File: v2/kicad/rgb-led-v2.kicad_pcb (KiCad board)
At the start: 2 copper layers, 90 x 50 mm, 11 parts

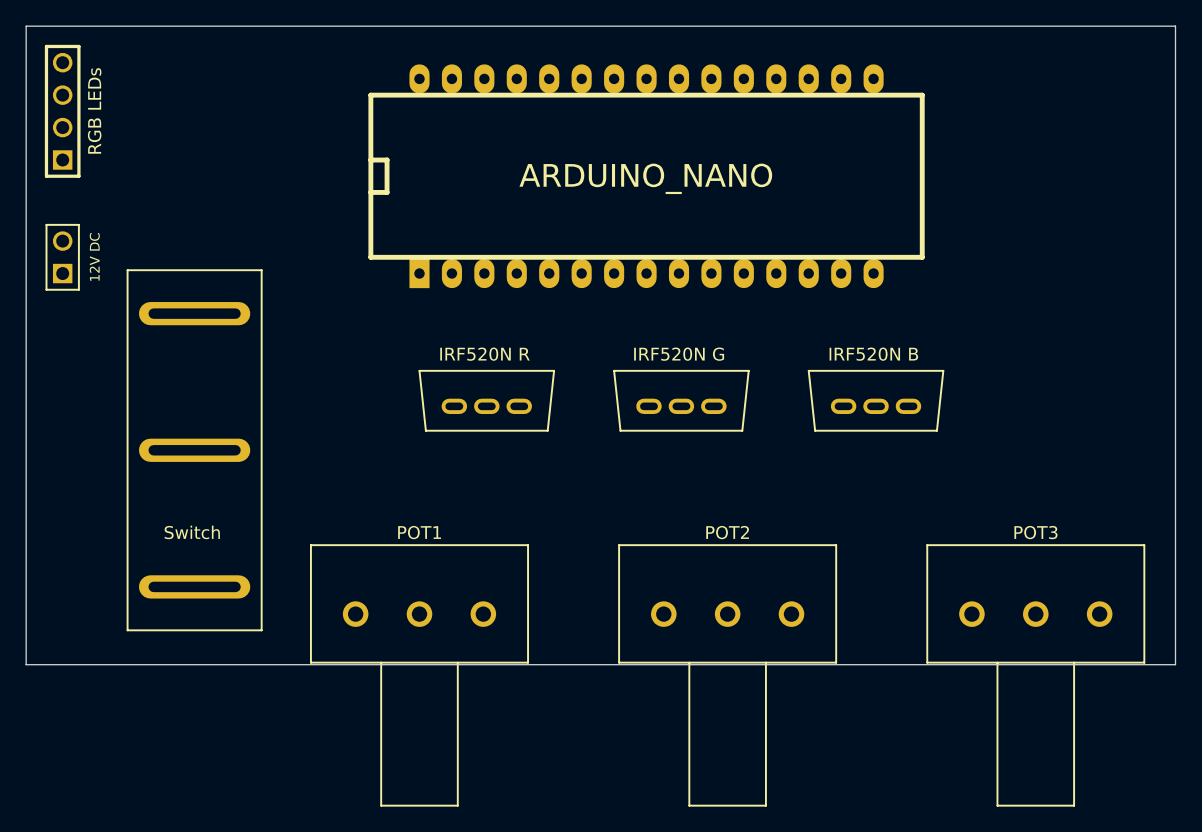
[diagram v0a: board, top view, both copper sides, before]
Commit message: [v2] Fixed references in PCB layout
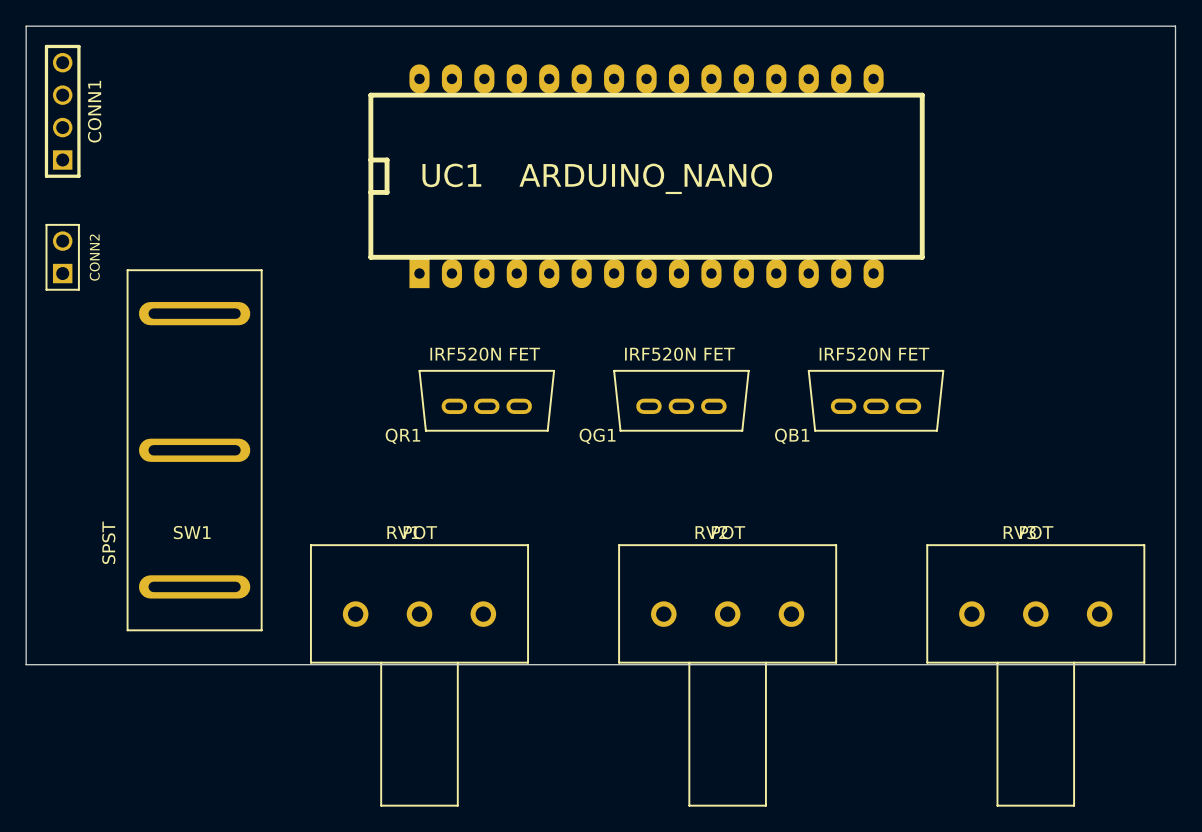
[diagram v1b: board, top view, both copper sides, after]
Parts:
- CONN1: renamed from RGB LEDs
- CONN2: renamed from 12V DC
- QB1: renamed from ?; value IRF520N B -> IRF520N FET
- QG1: renamed from ?; value IRF520N G -> IRF520N FET
- QR1: renamed from ?; value IRF520N R -> IRF520N FET
- RV1: renamed from ?; value POT1 -> POT
- RV2: renamed from ?; value POT2 -> POT
- RV3: renamed from ?; value POT3 -> POT
- SW1: renamed from Switch; value (none) -> SPST
- gave numbers to parts that had none: 1
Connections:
- QB1 pad D: (no net) -> N-0000016
- QB1 pad G: (no net) -> N-000004
- QB1 pad S: (no net) -> GND
- QG1 pad D: (no net) -> N-000005
- QG1 pad G: (no net) -> N-000001
- QG1 pad S: (no net) -> GND
- QR1 pad D: (no net) -> N-0000011
- QR1 pad G: (no net) -> N-000003
- QR1 pad S: (no net) -> GND
- SW1 pad 1: (no net) -> N-0000019
- SW1 pad 2: (no net) -> N-0000017
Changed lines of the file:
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@@
 (kicad_pcb (version 3) (host pcbnew "(2013-may-18)-stable")
   (general
-    (links 11)
-    (no_connects 11)
+    (links 22)
+    (no_connects 22)
     (area 18.679999 19.949999 115.369049 81.130001)
     (thickness 1.6)
@@
   (module POT_3 (layer F.Cu)
     (at 49.53 66.04)
-    (fp_text reference "" (at -1.27 -6.35) (layer F.SilkS)
-      (effects (font (size 1 1) (thickness 0.15)))
-    )
-    (fp_text value POT1 (at 0 -6.35) (layer F.SilkS)
+    (fp_text reference RV1 (at -1.27 -6.35) (layer F.SilkS)
+      (effects (font (size 1 1) (thickness 0.15)))
+    )
+    (fp_text value POT (at 0 -6.35) (layer F.SilkS)
       (effects (font (size 1 1) (thickness 0.15)))
     )
@@
   (module POT_3 (layer F.Cu)
     (at 73.66 66.04)
-    (fp_text reference "" (at -1.27 -6.35) (layer F.SilkS)
-      (effects (font (size 1 1) (thickness 0.15)))
-    )
-    (fp_text value POT2 (at 0 -6.35) (layer F.SilkS)
+    (fp_text reference RV2 (at -1.27 -6.35) (layer F.SilkS)
+      (effects (font (size 1 1) (thickness 0.15)))
+    )
+    (fp_text value POT (at 0 -6.35) (layer F.SilkS)
       (effects (font (size 1 1) (thickness 0.15)))
     )
@@
   (module POT_3 (layer F.Cu)
     (at 97.79 66.04)
-    (fp_text reference "" (at -1.27 -6.35) (layer F.SilkS)
-      (effects (font (size 1 1) (thickness 0.15)))
-    )
-    (fp_text value POT3 (at 0 -6.35) (layer F.SilkS)
+    (fp_text reference RV3 (at -1.27 -6.35) (layer F.SilkS)
+      (effects (font (size 1 1) (thickness 0.15)))
+    )
+    (fp_text value POT (at 0 -6.35) (layer F.SilkS)
       (effects (font (size 1 1) (thickness 0.15)))
     )
@@
     (descr "Double rangee de contacts 2 x 5 pins")
     (tags CONN)
-    (fp_text reference "RGB LEDs" (at 0 2.54 90) (layer F.SilkS)
+    (fp_text reference CONN1 (at 0 2.54 90) (layer F.SilkS)
       (effects (font (size 1.016 1.016) (thickness 0.2032)))
     )
@@
     (descr "Connecteurs 2 pins")
     (tags "CONN DEV")
-    (fp_text reference "12V DC" (at 0 2.54 90) (layer F.SilkS)
+    (fp_text reference CONN2 (at 0 2.54 90) (layer F.SilkS)
       (effects (font (size 0.762 0.762) (thickness 0.1524)))
     )
@@
   (module KCD3 (layer F.Cu)
     (at 26.67 67.31 90)
-    (fp_text reference Switch (at 7.62 5.08 180) (layer F.SilkS)
-      (effects (font (size 1 1) (thickness 0.15)))
-    )
-    (fp_text value "" (at 6.8072 -1.4351 90) (layer F.SilkS)
+    (fp_text reference SW1 (at 7.62 5.08 180) (layer F.SilkS)
+      (effects (font (size 1 1) (thickness 0.15)))
+    )
+    (fp_text value SPST (at 6.8072 -1.4351 90) (layer F.SilkS)
       (effects (font (size 1 1) (thickness 0.15)))
     )
@@
     (pad 1 thru_hole oval (at 3.4 5.25 90) (size 1.82 8.72) (drill oval 0.82 7.22)
       (layers *.Cu *.Mask F.SilkS)
+      (net 9 N-0000019)
     )
     (pad 2 thru_hole oval (at 14.1 5.25 90) (size 1.82 8.72) (drill oval 0.82 7.22)
       (layers *.Cu *.Mask F.SilkS)
+      (net 8 N-0000017)
     )
     (pad 3 thru_hole oval (at 24.8 5.25 90) (size 1.82 8.72) (drill oval 0.82 7.22)
@@
     (descr "30 pins DIL package, elliptical pads, width 600mil (arduino nano)")
     (tags "DIL arduino nano")
-    (fp_text reference "" (at -16.51 0) (layer F.SilkS)
+    (fp_text reference UC1 (at -16.51 0) (layer F.SilkS)
       (effects (font (size 1.778 1.778) (thickness 0.3048)))
     )
@@
   (module IRF520N (layer F.Cu)
     (at 49.53 46.99)
-    (fp_text reference "" (at -1.27 5.08) (layer F.SilkS)
-      (effects (font (size 1 1) (thickness 0.15)))
-    )
-    (fp_text value "IRF520N R" (at 5.08 -1.27) (layer F.SilkS)
+    (fp_text reference QR1 (at -1.27 5.08) (layer F.SilkS)
+      (effects (font (size 1 1) (thickness 0.15)))
+    )
+    (fp_text value "IRF520N FET" (at 5.08 -1.27) (layer F.SilkS)
       (effects (font (size 1 1) (thickness 0.15)))
     )
@@
     (pad G thru_hole oval (at 2.73 2.78) (size 2 1.2) (drill oval 1.4 0.6)
       (layers *.Cu *.Mask F.SilkS)
+      (net 11 N-000003)
     )
     (pad D thru_hole oval (at 5.27 2.78) (size 2 1.2) (drill oval 1.4 0.6)
       (layers *.Cu *.Mask F.SilkS)
+      (net 4 N-0000011)
     )
     (pad S thru_hole oval (at 7.81 2.78) (size 2 1.2) (drill oval 1.4 0.6)
       (layers *.Cu *.Mask F.SilkS)
+      (net 1 GND)
     )
   )
   (module IRF520N (layer F.Cu)
     (at 64.77 46.99)
-    (fp_text reference "" (at -1.27 5.08) (layer F.SilkS)
-      (effects (font (size 1 1) (thickness 0.15)))
-    )
-    (fp_text value "IRF520N G" (at 5.08 -1.27) (layer F.SilkS)
+    (fp_text reference QG1 (at -1.27 5.08) (layer F.SilkS)
+      (effects (font (size 1 1) (thickness 0.15)))
+    )
+    (fp_text value "IRF520N FET" (at 5.08 -1.27) (layer F.SilkS)
       (effects (font (size 1 1) (thickness 0.15)))
     )
@@
     (pad G thru_hole oval (at 2.73 2.78) (size 2 1.2) (drill oval 1.4 0.6)
       (layers *.Cu *.Mask F.SilkS)
+      (net 2 N-000001)
     )
     (pad D thru_hole oval (at 5.27 2.78) (size 2 1.2) (drill oval 1.4 0.6)
       (layers *.Cu *.Mask F.SilkS)
+      (net 13 N-000005)
     )
     (pad S thru_hole oval (at 7.81 2.78) (size 2 1.2) (drill oval 1.4 0.6)
       (layers *.Cu *.Mask F.SilkS)
+      (net 1 GND)
     )
   )
   (module IRF520N (layer F.Cu)
     (at 80.01 46.99)
-    (fp_text reference "" (at -1.27 5.08) (layer F.SilkS)
-      (effects (font (size 1 1) (thickness 0.15)))
-    )
-    (fp_text value "IRF520N B" (at 5.08 -1.27) (layer F.SilkS)
+    (fp_text reference QB1 (at -1.27 5.08) (layer F.SilkS)
+      (effects (font (size 1 1) (thickness 0.15)))
+    )
+    (fp_text value "IRF520N FET" (at 5.08 -1.27) (layer F.SilkS)
       (effects (font (size 1 1) (thickness 0.15)))
     )
@@
     (pad G thru_hole oval (at 2.73 2.78) (size 2 1.2) (drill oval 1.4 0.6)
       (layers *.Cu *.Mask F.SilkS)
+      (net 12 N-000004)
     )
     (pad D thru_hole oval (at 5.27 2.78) (size 2 1.2) (drill oval 1.4 0.6)
       (layers *.Cu *.Mask F.SilkS)
+      (net 7 N-0000016)
     )
     (pad S thru_hole oval (at 7.81 2.78) (size 2 1.2) (drill oval 1.4 0.6)
       (layers *.Cu *.Mask F.SilkS)
-    )
-  )
+      (net 1 GND)
+    )
+  )

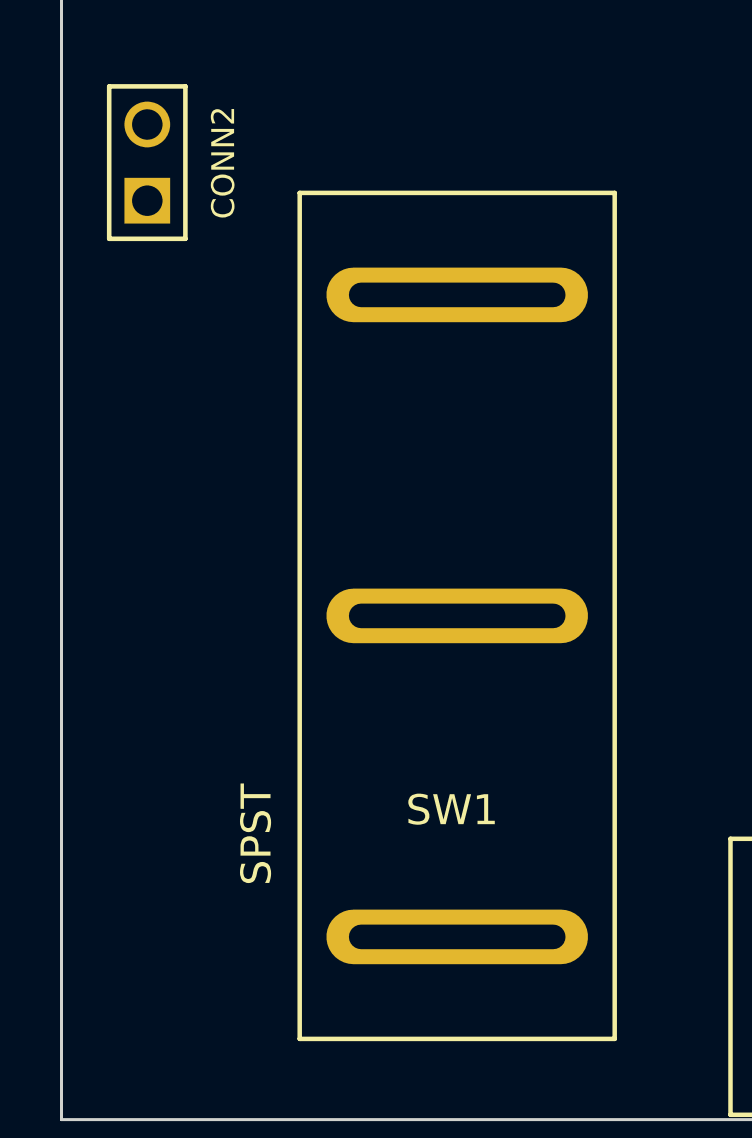
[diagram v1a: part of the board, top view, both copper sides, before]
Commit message: [v2] Configured track widths
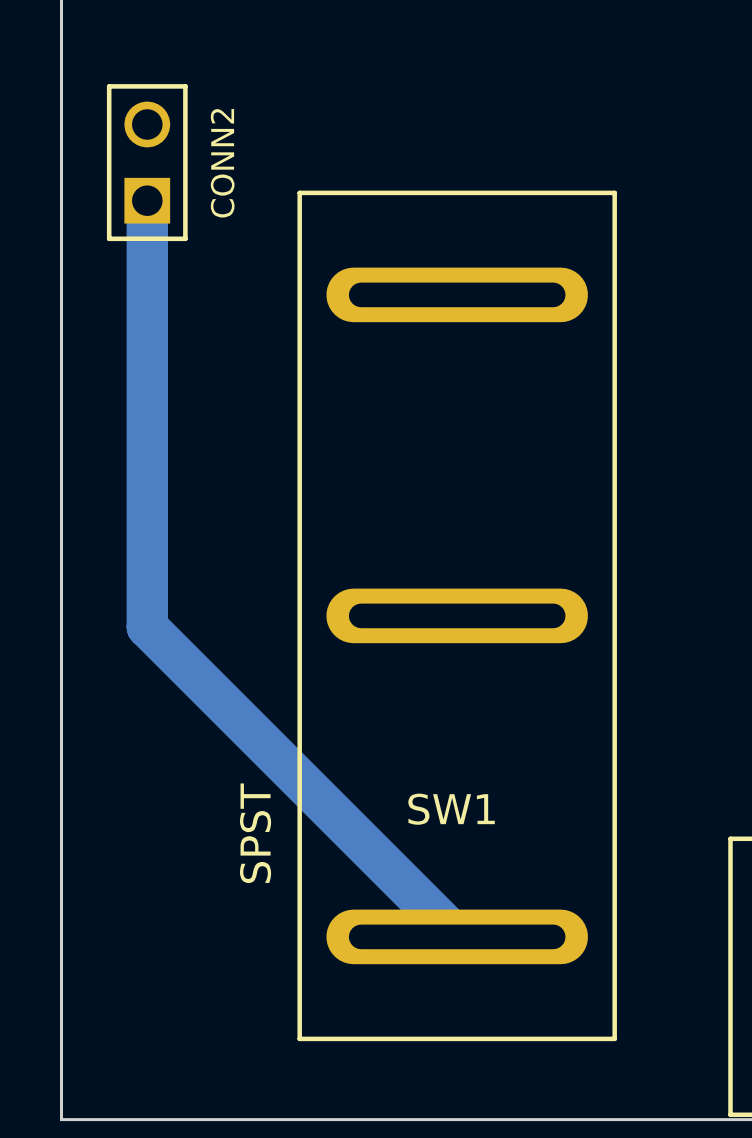
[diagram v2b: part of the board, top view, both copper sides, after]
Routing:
- net N-0000019: track 0.00 -> 28.8 mm
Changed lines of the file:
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@@
   (general
     (links 22)
-    (no_connects 22)
+    (no_connects 21)
     (area 18.679999 19.949999 115.369049 81.130001)
     (thickness 1.6)
     (drawings 6)
-    (tracks 0)
+    (tracks 2)
     (zones 0)
     (modules 11)
@@
   )
   (setup
-    (last_trace_width 0.01)
+    (last_trace_width 1.38)
+    (user_trace_width 0.035)
+    (user_trace_width 0.35)
+    (user_trace_width 1.38)
     (trace_clearance 0.015)
     (zone_clearance 0.508)
@@
   (gr_line (start 108.73 20) (end 108.73 70) (angle 90) (layer Edge.Cuts) (width 0.1))
   (gr_line (start 18.73 70) (end 108.73 70) (angle 90) (layer Edge.Cuts) (width 0.1))
+  (segment (start 21.59 39.37) (end 21.59 53.58) (width 1.38) (layer B.Cu) (net 9) (status 400000))
+  (segment (start 21.59 53.58) (end 31.92 63.91) (width 1.38) (layer B.Cu) (net 9) (status 800000))
 )

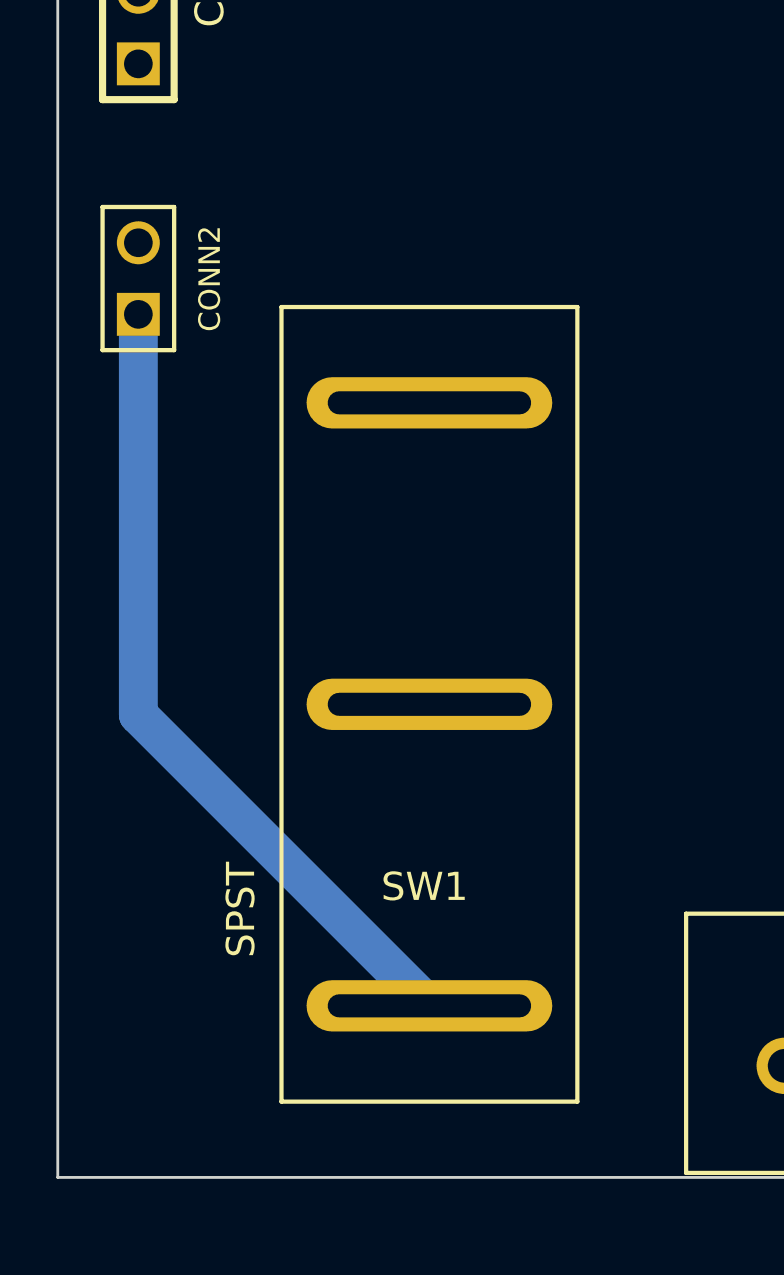
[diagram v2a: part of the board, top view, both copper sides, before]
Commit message: [v2] Added fuse
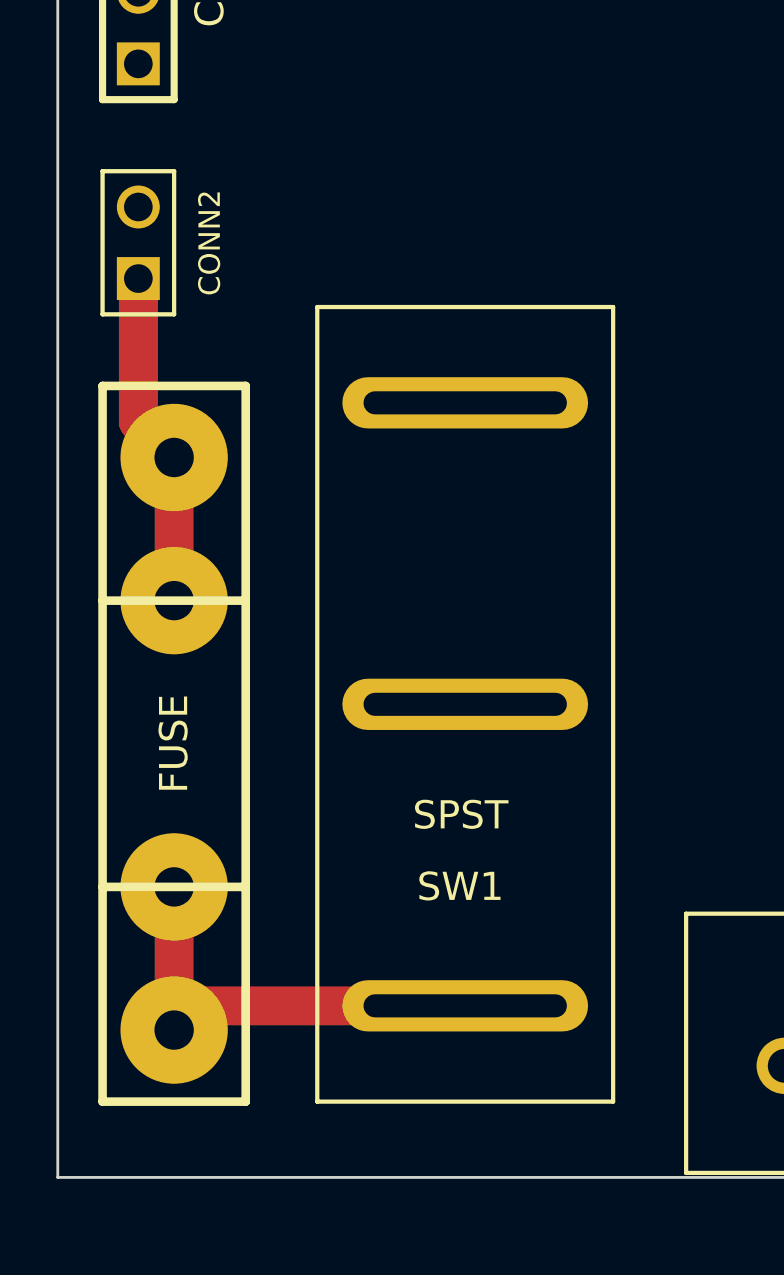
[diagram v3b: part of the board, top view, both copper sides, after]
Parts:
- added F1: FUSE, FUSE5-20, F.Cu at (22.9, 54.6)
- moved CONN2 1.27 mm to (21.6, 36.8)
- moved SW1 1.27 mm to (27.9, 67.3)
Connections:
- CONN2 pad 1: N-0000019 -> N-000009
- SW1 pad 1: N-0000019 -> N-000002
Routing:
- net N-0000019: track 28.8 -> 0.00 mm
- net N-000002: track 0.00 -> 15.8 mm
- net N-000009: track 0.00 -> 12.0 mm

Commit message: [v2] PCB Routing
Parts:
- moved QB1 15.2 mm to (64.8, 47.0)
- moved QG1 15.2 mm to (80.0, 47.0)
- moved G*** 3.17 mm to (36.8, 28.6)
- turned UC1 to 180 degrees
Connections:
- CONN1 pad 1: N-000008 (its old number) -> N-000007
- SW1 pad 2: N-000008 (its old number) -> N-000007
- UC1 pad 15: (no net) -> N-000007
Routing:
- net N-000001: track 0.00 -> 125.6 mm, vias 0 -> 2
- net N-000003: track 0.00 -> 99.3 mm
- net N-000004: track 0.00 -> 80.8 mm
- net N-0000012: track 0.00 -> 72.8 mm
- net N-000005: track 0.00 -> 67.0 mm
- net N-000007: track 0.00 -> 65.6 mm, vias 0 -> 2
- net N-0000014: track 0.00 -> 61.1 mm, vias 0 -> 2
- net N-0000013: track 0.00 -> 45.6 mm, vias 0 -> 2
- net N-000009: track 0.00 -> 19.2 mm
- net N-0000011: track 0.00 -> 17.0 mm
- net N-0000010: track 0.00 -> 11.4 mm
- added copper zone on F.Cu, net GND

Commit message: [v2] Improved PCB
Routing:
- net N-000001: track 125.6 -> 135.5 mm, vias 2 -> 0
- net N-000007: track 65.6 -> 64.5 mm
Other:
- board text added: "+"
- board text added: "1"
- board text added: "12V"
- board text added: "15"
- board text added: "16"
- board text added: "30"
- board text added: "Arduino Nano v3"
- board text added: "B"
- board text added: "Fuse 3A"
- board text added: "G"
- board text added: "GND"
- board text added: "IRF520N"
- board text added: "R"
- board text added: "RV1"
- board text added: "RV2"
- board text added: "RV3"
- board text added: "USB"
